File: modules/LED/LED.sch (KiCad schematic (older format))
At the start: 54 parts, among them J1 2, J10 11, J11 12, J12 13, J13 A0, J14 A1, J15 A2, J16 A3, J17 A4, J18 A5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

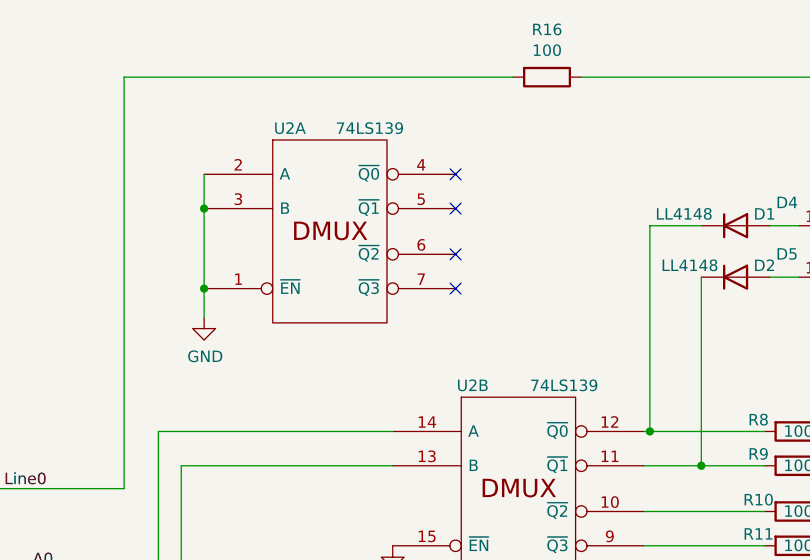
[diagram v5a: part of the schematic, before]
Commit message: Fix 74LS139 pins
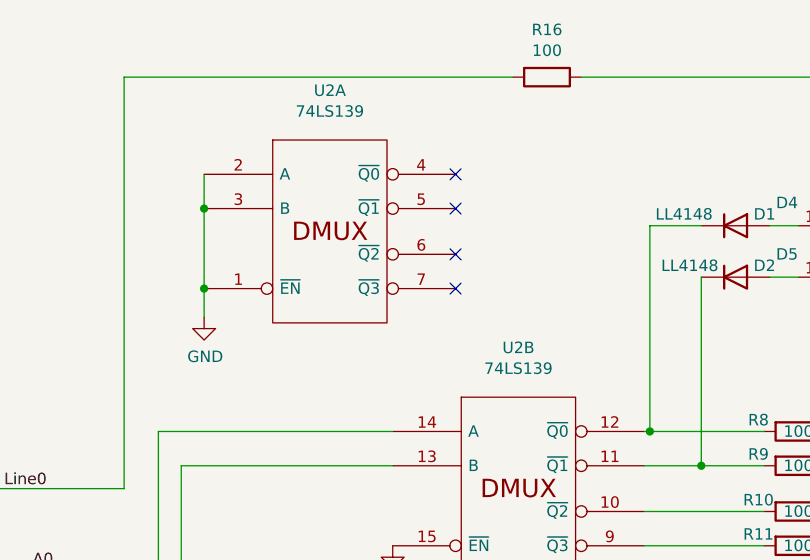
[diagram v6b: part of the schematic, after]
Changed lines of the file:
@@
 EESchema Schematic File Version 4
-LIBS:LED-cache
 EELAYER 30 0
 EELAYER END
@@
 CA
 $Comp
-L 74xx_IEEE:74LS139 U2
-U 2 1 5D9F2012
-P 3725 2800
-F 0 "U2" H 3525 3250 50  0000 C CNN
-F 1 "74LS139" H 3925 3250 50  0000 C CNN
-F 2 "Package_SO:SOIC-16_3.9x9.9mm_P1.27mm" H 3725 2800 50  0001 C CNN
-F 3 "" H 3725 2800 50  0001 C CNN
-	2    3725 2800
-	1    0    0    -1
-$EndComp
-$Comp
-L 74xx_IEEE:74LS139 U2
-U 1 1 5D9F2921
-P 2900 1675
-F 0 "U2" H 2725 2125 50  0000 C CNN
-F 1 "74LS139" H 3075 2125 50  0000 C CNN
-F 2 "Package_SO:SOIC-16_3.9x9.9mm_P1.27mm" H 2900 1675 50  0001 C CNN
-F 3 "" H 2900 1675 50  0001 C CNN
-	1    2900 1675
-	1    0    0    -1
-$EndComp
-$Comp
 L 74xx:74LS247 U1
 U 1 1 5D9F3F2D
@@
 	1    0    0    -1
 $EndComp
-Wire Wire Line
-	2350 1425 2350 1575
-Wire Wire Line
-	2350 1575 2350 1925
-Connection ~ 2350 1575
-Wire Wire Line
-	2350 1925 2350 2050
-Connection ~ 2350 1925
 NoConn ~ 3150 4950
 NoConn ~ 3450 1425
@@
 Wire Wire Line
 	2000 1000 3700 1000
-Wire Wire Line
-	4000 1000 5600 1000
 $Comp
 L Device:Jumper JP1
@@
 	2675 5650 3300 5650
 Connection ~ 3300 5650
+$Comp
+L 74xx_IEEE:74LS139 U2
+U 1 1 5FA62F1E
+P 2900 1675
+F 0 "U2" H 2900 2291 50  0000 C CNN
+F 1 "74LS139" H 2900 2200 50  0000 C CNN
+F 2 "Package_SO:SOIC-16_3.9x9.9mm_P1.27mm" H 2900 1675 50  0001 C CNN
+F 3 "http://www.ti.com/lit/ds/symlink/sn74ls139a.pdf" H 2900 1675 50  0001 C CNN
+	1    2900 1675
+	1    0    0    -1
+$EndComp
+$Comp
+L 74xx_IEEE:74LS139 U2
+U 2 1 5FA64326
+P 3725 2800
+F 0 "U2" H 3725 3416 50  0000 C CNN
+F 1 "74LS139" H 3725 3325 50  0000 C CNN
+F 2 "Package_SO:SOIC-16_3.9x9.9mm_P1.27mm" H 3725 2800 50  0001 C CNN
+F 3 "http://www.ti.com/lit/ds/symlink/sn74ls139a.pdf" H 3725 2800 50  0001 C CNN
+	2    3725 2800
+	1    0    0    -1
+$EndComp
+Wire Wire Line
+	2350 1425 2350 1575
+Wire Wire Line
+	2350 2050 2350 1925
+Wire Wire Line
+	4000 1000 5600 1000
+Wire Wire Line
+	2350 1925 2350 1575
+Connection ~ 2350 1925
+Connection ~ 2350 1575
 $EndSCHEMATC
